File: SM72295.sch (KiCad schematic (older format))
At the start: 22 parts, among them U4 SM72295

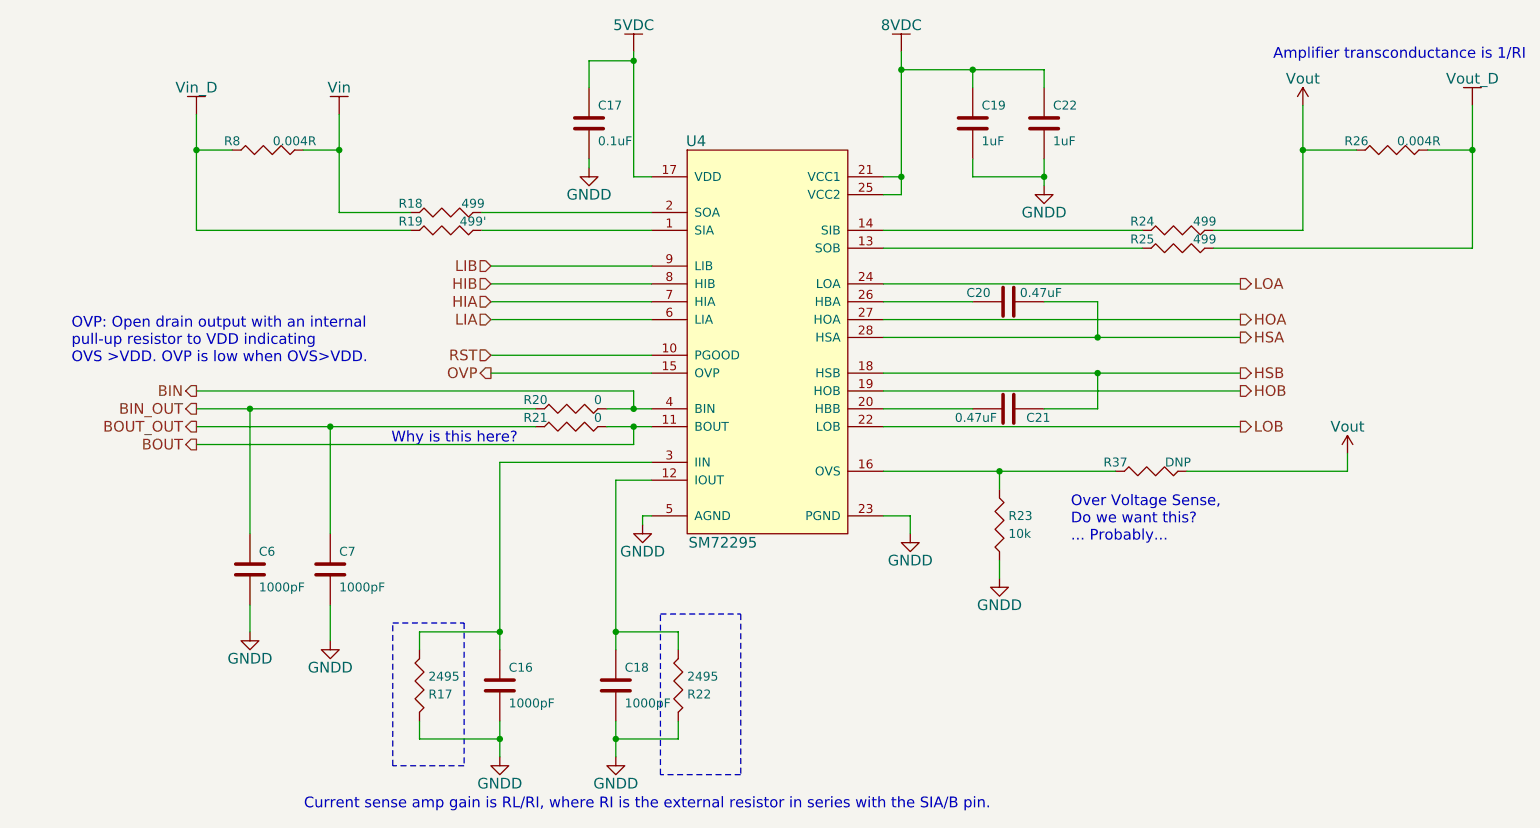
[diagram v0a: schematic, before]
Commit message: Started placing components
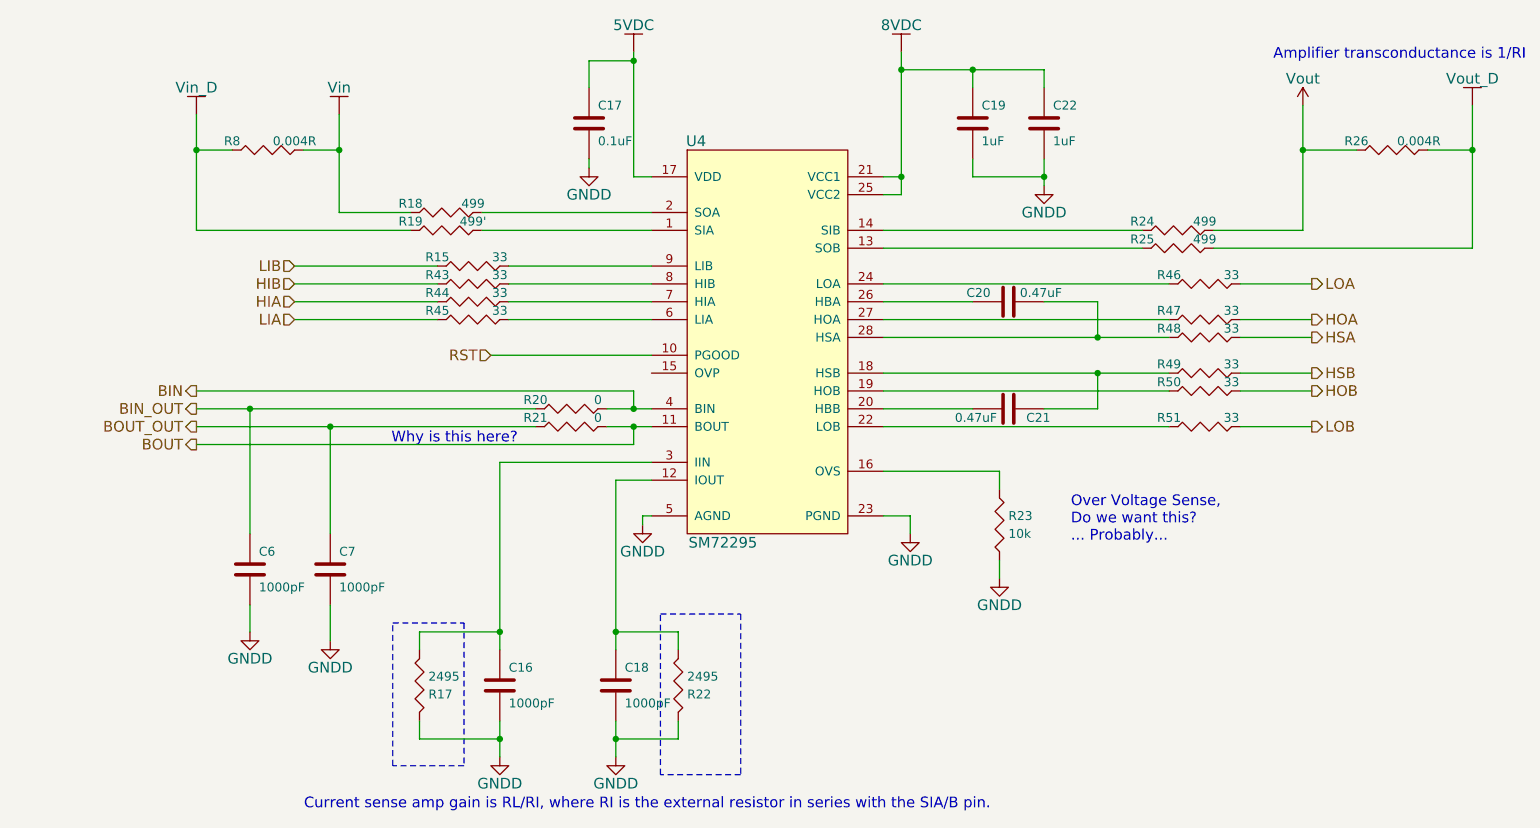
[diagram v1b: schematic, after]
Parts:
- removed R37: DNP, Resistors_SMD:R_0805_HandSoldering, symbol Rh
- added R15: 33, Resistors_SMD:R_0805_HandSoldering, symbol Rh
- added R43, R44, R45, R46, R47, R48, R49, R50, R51: 33, Resistors_SMD:R_0603_HandSoldering, symbol Rh
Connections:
- net HIA: now also R44.1; no longer U4.7 (HIA)
- net HIB: now also R43.1; no longer U4.8 (HIB)
- net HOA: now also R47.2; no longer U4.27 (HOA)
- net HOB: now also R50.2; no longer U4.19 (HOB)
- net HSA: now also R48.2; no longer C20.2, U4.28 (HSA)
- net HSB: now also R49.2; no longer C21.1, U4.18 (HSB)
- net LIA: now also R45.1; no longer U4.6 (LIA)
- net LIB: now also R15.1; no longer U4.9 (LIB)
- net LOA: now also R46.2; no longer U4.24 (LOA)
- net LOB: now also R51.2; no longer U4.22 (LOB)
- net OVP: no longer names the net of U4.15 (OVP)
- new net: C21.1, R49.1, U4.18 (HSB)
- new net: R50.1, U4.19 (HOB)
- new net: R51.1, U4.22 (LOB)
- new net: R46.1, U4.24 (LOA)
- new net: R47.1, U4.27 (HOA)
- new net: C20.2, R48.1, U4.28 (HSA)
- new net: R45.2, U4.6 (LIA)
- new net: R44.2, U4.7 (HIA)
- new net: R43.2, U4.8 (HIB)
- new net: R15.2, U4.9 (LIB)
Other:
- note removed: "OVP: Open drain output with an internal\npull-up resistor to VDD indicating \nOVS >VDD. OVP is low when OVS>VDD."

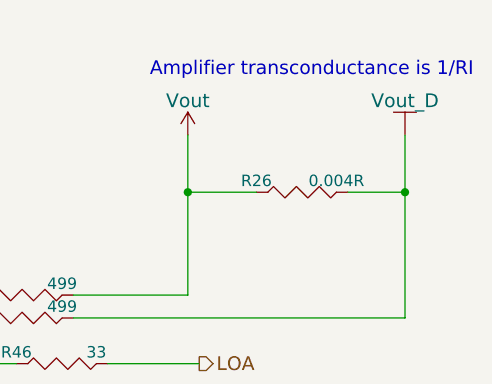
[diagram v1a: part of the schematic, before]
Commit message: still trying to get initial placements done.  Still need to fine-tune
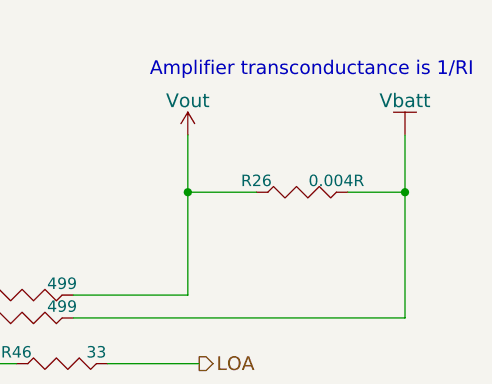
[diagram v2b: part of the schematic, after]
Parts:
- C16, C17, C18, C19, C20, C21, C22, C6, C7: footprint Capacitors_SMD:C_0805_HandSoldering -> Capacitors_SMD:C_0603_HandSoldering
- R15, R17, R18, R19, R20, R21, R22, R23, R24, R25, R26, R8: footprint Resistors_SMD:R_0805_HandSoldering -> Resistors_SMD:R_0603_HandSoldering
- U4: footprint Housings_SSOP:TSSOP-28_4.4x9.7mm_Pitch0.65mm -> Housings_SOIC:SOIC-28_7.5x17.9mm_Pitch1.27mm
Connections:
- net Vout_D renamed Vbatt
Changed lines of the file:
@@
 F 0 "C19" H 6500 2250 50  0000 L CNN
 F 1 "1uF" H 6500 2050 50  0000 L CNN
-F 2 "Capacitors_SMD:C_0805_HandSoldering" H 6488 2000 30  0001 C CNN
+F 2 "Capacitors_SMD:C_0603_HandSoldering" H 6488 2000 30  0001 C CNN
 F 3 "" H 6450 2150 60  0000 C CNN
 	1    6450 2150
@@
 F 0 "C22" H 6900 2250 50  0000 L CNN
 F 1 "1uF" H 6900 2050 50  0000 L CNN
-F 2 "Capacitors_SMD:C_0805_HandSoldering" H 6888 2000 30  0001 C CNN
+F 2 "Capacitors_SMD:C_0603_HandSoldering" H 6888 2000 30  0001 C CNN
 F 3 "" H 6850 2150 60  0000 C CNN
 	1    6850 2150
@@
 F 0 "R24" H 7400 2800 50  0000 C CNN
 F 1 "499" H 7750 2800 50  0000 C CNN
-F 2 "Resistors_SMD:R_0805_HandSoldering" H 7600 2680 30  0001 C CNN
+F 2 "Resistors_SMD:R_0603_HandSoldering" H 7600 2680 30  0001 C CNN
 F 3 "" V 7600 2750 30  0000 C CNN
 	1    7600 2750
@@
 F 0 "R25" H 7400 2900 50  0000 C CNN
 F 1 "499" H 7750 2900 50  0000 C CNN
-F 2 "Resistors_SMD:R_0805_HandSoldering" H 7600 2780 30  0001 C CNN
+F 2 "Resistors_SMD:R_0603_HandSoldering" H 7600 2780 30  0001 C CNN
 F 3 "" V 7600 2850 30  0000 C CNN
 	1    7600 2850
@@
 F 0 "U4" H 4900 4150 60  0000 C CNN
 F 1 "SM72295" H 5050 1900 60  0000 C CNN
-F 2 "Housings_SSOP:TSSOP-28_4.4x9.7mm_Pitch0.65mm" H 5300 3200 60  0001 C CNN
+F 2 "Housings_SOIC:SOIC-28_7.5x17.9mm_Pitch1.27mm" H 5300 3200 60  0001 C CNN
 F 3 "" H 5300 3200 60  0000 C CNN
 	1    5300 3200
@@
 F 0 "R18" H 3300 2700 50  0000 C CNN
 F 1 "499" H 3650 2700 50  0000 C CNN
-F 2 "Resistors_SMD:R_0805_HandSoldering" H 3500 2580 30  0001 C CNN
+F 2 "Resistors_SMD:R_0603_HandSoldering" H 3500 2580 30  0001 C CNN
 F 3 "" V 3500 2650 30  0000 C CNN
 	1    3500 2650
@@
 F 0 "R19" H 3300 2800 50  0000 C CNN
 F 1 "499'" H 3650 2800 50  0000 C CNN
-F 2 "Resistors_SMD:R_0805_HandSoldering" H 3500 2680 30  0001 C CNN
+F 2 "Resistors_SMD:R_0603_HandSoldering" H 3500 2680 30  0001 C CNN
 F 3 "" V 3500 2750 30  0000 C CNN
 	1    3500 2750
@@
 F 0 "C17" H 4350 2250 50  0000 L CNN
 F 1 "0.1uF" H 4350 2050 50  0000 L CNN
-F 2 "Capacitors_SMD:C_0805_HandSoldering" H 4338 2000 30  0001 C CNN
+F 2 "Capacitors_SMD:C_0603_HandSoldering" H 4338 2000 30  0001 C CNN
 F 3 "" H 4300 2150 60  0000 C CNN
 	1    4300 2150
@@
 F 0 "R21" H 4000 3900 50  0000 C CNN
 F 1 "0" H 4350 3900 50  0000 C CNN
-F 2 "Resistors_SMD:R_0805_HandSoldering" H 4200 3780 30  0001 C CNN
+F 2 "Resistors_SMD:R_0603_HandSoldering" H 4200 3780 30  0001 C CNN
 F 3 "" V 4200 3850 30  0000 C CNN
 	1    4200 3850
@@
 F 0 "R20" H 4000 3800 50  0000 C CNN
 F 1 "0" H 4350 3800 50  0000 C CNN
-F 2 "Resistors_SMD:R_0805_HandSoldering" H 4200 3680 30  0001 C CNN
+F 2 "Resistors_SMD:R_0603_HandSoldering" H 4200 3680 30  0001 C CNN
 F 3 "" V 4200 3750 30  0000 C CNN
 	1    4200 3750
@@
 F 0 "C6" H 2450 4750 50  0000 L CNN
 F 1 "1000pF" H 2450 4550 50  0000 L CNN
-F 2 "Capacitors_SMD:C_0805_HandSoldering" H 2438 4500 30  0001 C CNN
+F 2 "Capacitors_SMD:C_0603_HandSoldering" H 2438 4500 30  0001 C CNN
 F 3 "" H 2400 4650 60  0000 C CNN
 	1    2400 4650
@@
 F 0 "C7" H 2900 4750 50  0000 L CNN
 F 1 "1000pF" H 2900 4550 50  0000 L CNN
-F 2 "Capacitors_SMD:C_0805_HandSoldering" H 2888 4500 30  0001 C CNN
+F 2 "Capacitors_SMD:C_0603_HandSoldering" H 2888 4500 30  0001 C CNN
 F 3 "" H 2850 4650 60  0000 C CNN
 	1    2850 4650
@@
 F 0 "C20" V 6700 3250 50  0000 L CNN
 F 1 "0.47uF" V 6700 2850 50  0000 L CNN
-F 2 "Capacitors_SMD:C_0805_HandSoldering" H 6688 3000 30  0001 C CNN
+F 2 "Capacitors_SMD:C_0603_HandSoldering" H 6688 3000 30  0001 C CNN
 F 3 "" H 6650 3150 60  0000 C CNN
 	1    6650 3150
@@
 F 0 "C21" V 6700 3850 50  0000 L CNN
 F 1 "0.47uF" V 6700 3450 50  0000 L CNN
-F 2 "Capacitors_SMD:C_0805_HandSoldering" H 6688 3600 30  0001 C CNN
+F 2 "Capacitors_SMD:C_0603_HandSoldering" H 6688 3600 30  0001 C CNN
 F 3 "" H 6650 3750 60  0000 C CNN
 	1    6650 3750
@@
 F 0 "C16" H 3850 5400 50  0000 L CNN
 F 1 "1000pF" H 3850 5200 50  0000 L CNN
-F 2 "Capacitors_SMD:C_0805_HandSoldering" H 3838 5150 30  0001 C CNN
+F 2 "Capacitors_SMD:C_0603_HandSoldering" H 3838 5150 30  0001 C CNN
 F 3 "" H 3800 5300 60  0000 C CNN
 	1    3800 5300
@@
 F 0 "R17" H 3400 5350 50  0000 L CNN
 F 1 "2495" H 3400 5250 50  0000 L CNN
-F 2 "Resistors_SMD:R_0805_HandSoldering" V 3280 5300 30  0001 C CNN
+F 2 "Resistors_SMD:R_0603_HandSoldering" V 3280 5300 30  0001 C CNN
 F 3 "" H 3350 5300 30  0000 C CNN
 	1    3350 5300
@@
 F 0 "C18" H 4500 5400 50  0000 L CNN
 F 1 "1000pF" H 4500 5200 50  0000 L CNN
-F 2 "Capacitors_SMD:C_0805_HandSoldering" H 4488 5150 30  0001 C CNN
+F 2 "Capacitors_SMD:C_0603_HandSoldering" H 4488 5150 30  0001 C CNN
 F 3 "" H 4450 5300 60  0000 C CNN
 	1    4450 5300
@@
 F 0 "R22" H 4850 5350 50  0000 L CNN
 F 1 "2495" H 4850 5250 50  0000 L CNN
-F 2 "Resistors_SMD:R_0805_HandSoldering" V 4730 5300 30  0001 C CNN
+F 2 "Resistors_SMD:R_0603_HandSoldering" V 4730 5300 30  0001 C CNN
 F 3 "" H 4800 5300 30  0000 C CNN
 	1    4800 5300
@@
 F 0 "R8" H 2300 2350 50  0000 C CNN
 F 1 "0.004R" H 2650 2350 50  0000 C CNN
-F 2 "Resistors_SMD:R_0805_HandSoldering" H 2500 2230 30  0001 C CNN
+F 2 "Resistors_SMD:R_0603_HandSoldering" H 2500 2230 30  0001 C CNN
 F 3 "" V 2500 2300 30  0000 C CNN
 	1    2500 2300
@@
 $EndComp
 $Comp
-L Vout_D #PWR047
-U 1 1 54F279FB
-P 9250 2050
-F 0 "#PWR047" H 9250 1900 60  0001 C CNN
-F 1 "Vout_D" H 9250 2200 60  0000 C CNN
-F 2 "" H 9250 2050 60  0000 C CNN
-F 3 "" H 9250 2050 60  0000 C CNN
-	1    9250 2050
-	1    0    0    -1
-$EndComp
-$Comp
-L Vout #PWR048
+L Vout #PWR047
 U 1 1 54F27A37
 P 8300 2050
-F 0 "#PWR048" H 8300 1900 60  0001 C CNN
+F 0 "#PWR047" H 8300 1900 60  0001 C CNN
 F 1 "Vout" H 8300 2200 60  0000 C CNN
 F 2 "" H 8300 2050 60  0000 C CNN
@@
 F 0 "R26" H 8600 2350 50  0000 C CNN
 F 1 "0.004R" H 8950 2350 50  0000 C CNN
-F 2 "Resistors_SMD:R_0805_HandSoldering" H 8800 2230 30  0001 C CNN
+F 2 "Resistors_SMD:R_0603_HandSoldering" H 8800 2230 30  0001 C CNN
 F 3 "" V 8800 2300 30  0000 C CNN
 	1    8800 2300
@@
 F 0 "R23" H 6650 4450 50  0000 L CNN
 F 1 "10k" H 6650 4350 50  0000 L CNN
-F 2 "Resistors_SMD:R_0805_HandSoldering" V 6530 4400 30  0001 C CNN
+F 2 "Resistors_SMD:R_0603_HandSoldering" V 6530 4400 30  0001 C CNN
 F 3 "" H 6600 4400 30  0000 C CNN
 	1    6600 4400
@@
 	6600 4100 6600 4200
 $Comp
-L GNDD #PWR049
+L GNDD #PWR048
 U 1 1 54F2A6E3
 P 6600 4700
-F 0 "#PWR049" H 6600 4450 60  0001 C CNN
+F 0 "#PWR048" H 6600 4450 60  0001 C CNN
 F 1 "GNDD" H 6600 4550 60  0000 C CNN
 F 2 "" H 6600 4700 60  0000 C CNN
@@
 BIN
 $Comp
-L 5VDC #PWR050
+L 5VDC #PWR049
 U 1 1 54F8B7CD
 P 4550 1750
-F 0 "#PWR050" H 4550 1600 60  0001 C CNN
+F 0 "#PWR049" H 4550 1600 60  0001 C CNN
 F 1 "5VDC" H 4550 1900 60  0000 C CNN
 F 2 "" H 4550 1750 60  0000 C CNN
@@
 F 0 "R15" H 3450 3000 50  0000 C CNN
 F 1 "33" H 3800 3000 50  0000 C CNN
-F 2 "Resistors_SMD:R_0805_HandSoldering" H 3650 2880 30  0001 C CNN
+F 2 "Resistors_SMD:R_0603_HandSoldering" H 3650 2880 30  0001 C CNN
 F 3 "" V 3650 2950 30  0000 C CNN
 	1    3650 2950
@@
 	1    0    0    -1
 $EndComp
+$Comp
+L Vbatt #PWR050
+U 1 1 54FF73F2
+P 9250 2050
+F 0 "#PWR050" H 9250 1900 60  0001 C CNN
+F 1 "Vbatt" H 9250 2200 60  0000 C CNN
+F 2 "" H 9250 2050 60  0000 C CNN
+F 3 "" H 9250 2050 60  0000 C CNN
+	1    9250 2050
+	1    0    0    -1
+$EndComp

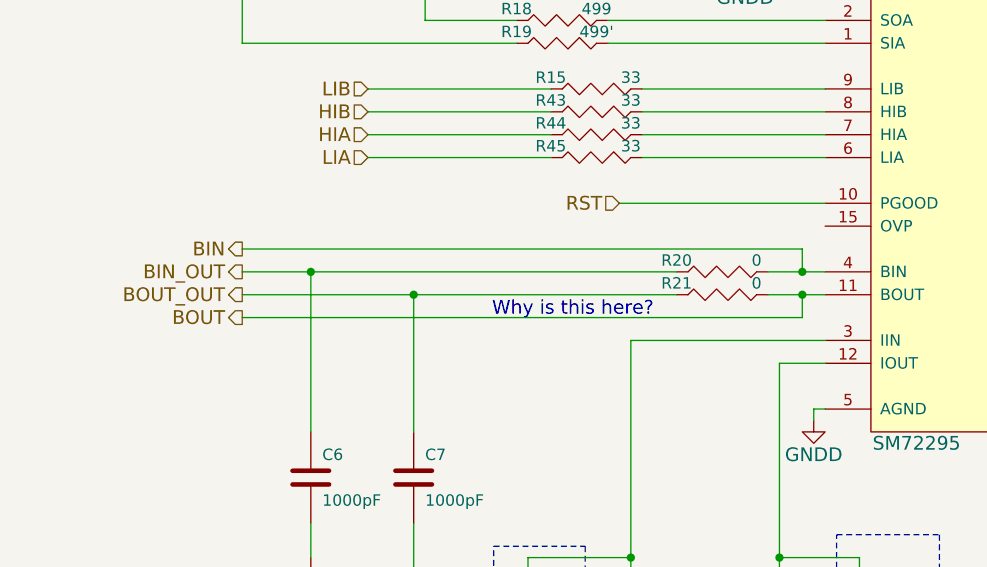
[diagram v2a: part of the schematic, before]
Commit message: Routing done, prepping for DRC
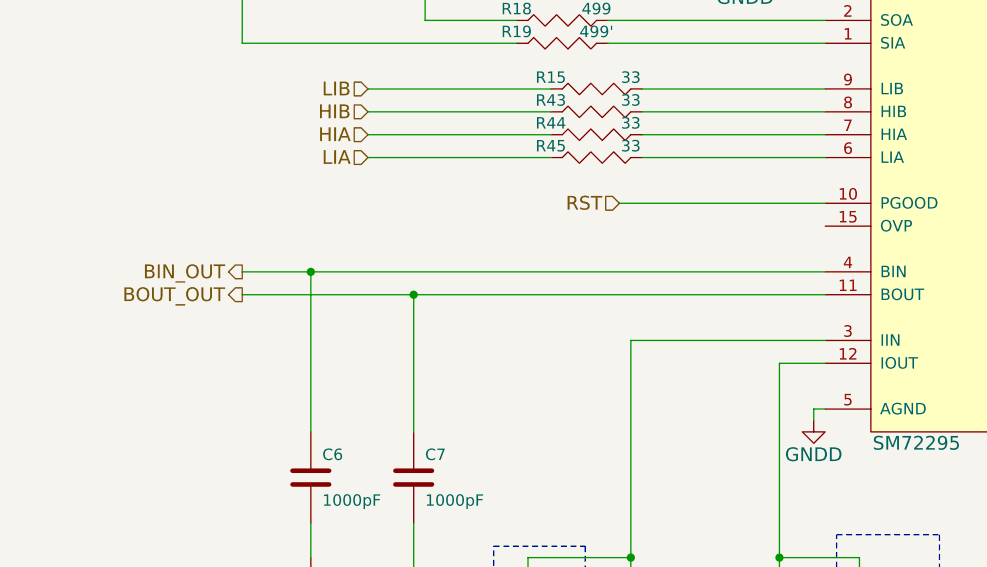
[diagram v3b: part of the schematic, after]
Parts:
- removed R20, R21: 0, Resistors_SMD:R_0603_HandSoldering, symbol Rh
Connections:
- net BIN is gone; now on net BIN_OUT: U4.4 (BIN)
- net BOUT is gone; now on net BOUT_OUT: U4.11 (BOUT)
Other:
- note removed: "Why is this here?"
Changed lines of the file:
@@
-	1    0    0    -1
-$EndComp
-$Comp
-L Rh R21
-U 1 1 54F0FFC1
-P 4200 3850
-F 0 "R21" H 4000 3900 50  0000 C CNN
-F 1 "0" H 4350 3900 50  0000 C CNN
-F 2 "Resistors_SMD:R_0603_HandSoldering" H 4200 3780 30  0001 C CNN
-F 3 "" V 4200 3850 30  0000 C CNN
-	1    4200 3850
-	1    0    0    -1
-$EndComp
-$Comp
-L Rh R20
-U 1 1 54F10058
-P 4200 3750
-F 0 "R20" H 4000 3800 50  0000 C CNN
-F 1 "0" H 4350 3800 50  0000 C CNN
-F 2 "Resistors_SMD:R_0603_HandSoldering" H 4200 3680 30  0001 C CNN
-F 3 "" V 4200 3750 30  0000 C CNN
-	1    4200 3750
 	1    0    0    -1
 $EndComp
@@
 	1    0    0    -1
 $EndComp
-Text HLabel 2100 3950 0    60   Output ~ 0
-BOUT
 $Comp
 L C C16
@@
 Text Notes 6550 6000 2    60   ~ 0
 Current sense amp gain is RL/RI, where RI is the external resistor in series with the SIA/B pin.
-Text Notes 3900 3950 2    60   ~ 0
-Why is this here?
 $Comp
 L Vin_D #PWR045
@@
 	2850 5050 2850 4850
 Wire Wire Line
-	2100 3850 4000 3850
+	2100 3850 4650 3850
 Wire Wire Line
 	2850 4450 2850 3850
@@
 	2400 4450 2400 3750
 Wire Wire Line
-	2100 3750 4000 3750
-Wire Wire Line
-	4400 3750 4650 3750
-Wire Wire Line
-	4400 3850 4650 3850
+	2100 3750 4650 3750
 Connection ~ 4550 1800
 Wire Wire Line
@@
 Wire Wire Line
 	3750 3450 4650 3450
-Wire Wire Line
-	2100 3950 4550 3950
-Wire Wire Line
-	4550 3950 4550 3850
-Connection ~ 4550 3850
 Wire Wire Line
 	3350 5000 3350 5100
@@
 Wire Wire Line
 	6600 4600 6600 4700
-Wire Wire Line
-	4550 3750 4550 3650
-Wire Wire Line
-	4550 3650 2100 3650
-Connection ~ 4550 3750
-Text HLabel 2100 3650 0    60   Output ~ 0
-BIN
 $Comp
 L 5VDC #PWR049

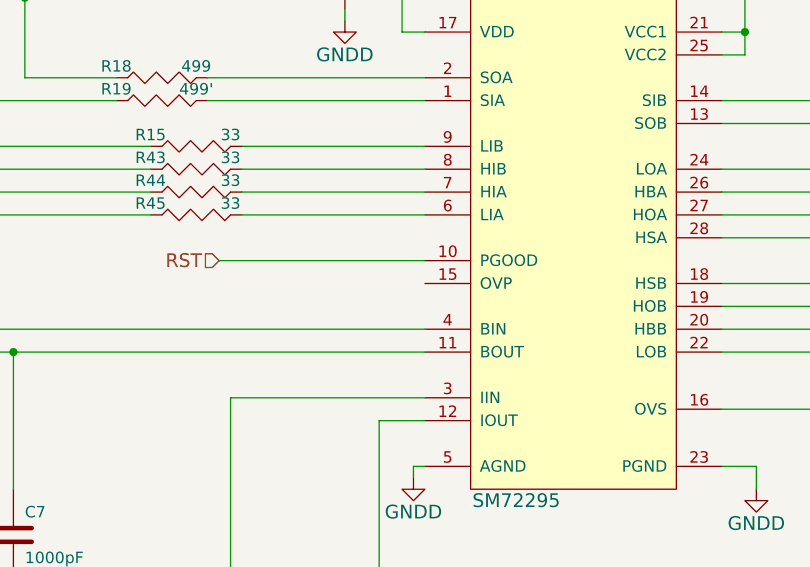
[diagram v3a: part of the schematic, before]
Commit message: Cleared all DRC errors.
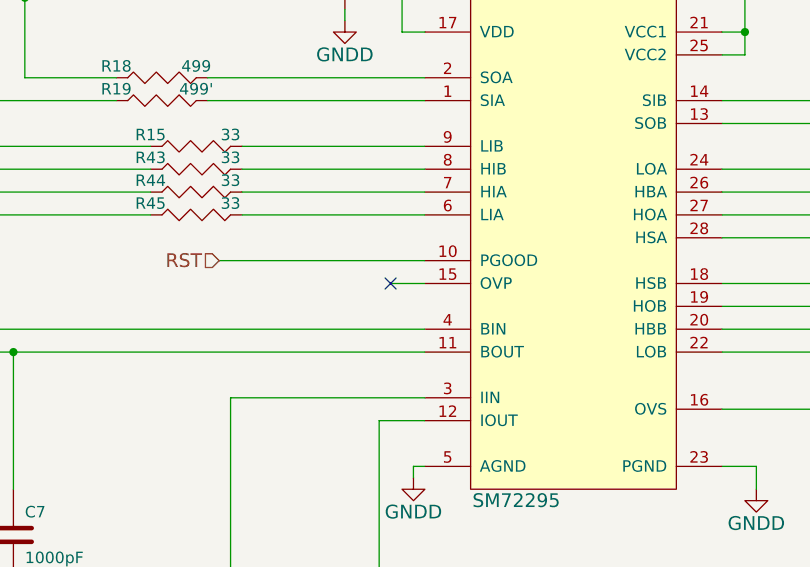
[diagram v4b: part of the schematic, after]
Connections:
- no-connect marks 0 -> 1
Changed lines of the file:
@@
 	1    0    0    -1
 $EndComp
+NoConn ~ 4500 3550
+Wire Wire Line
+	4500 3550 4650 3550
 $EndSCHEMATC
